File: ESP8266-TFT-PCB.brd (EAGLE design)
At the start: 38 x 50.8 mm, 5 parts

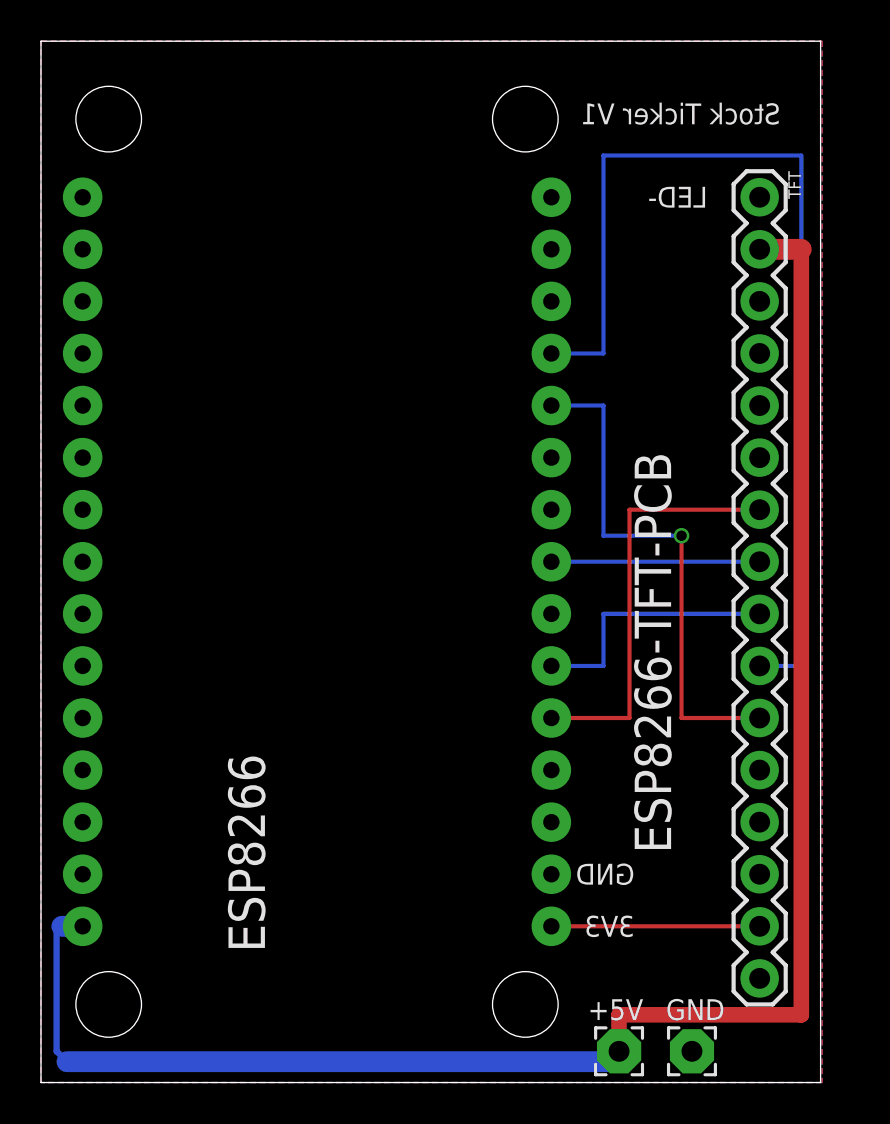
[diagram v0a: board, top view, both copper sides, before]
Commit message: Renamed and moved power connectors
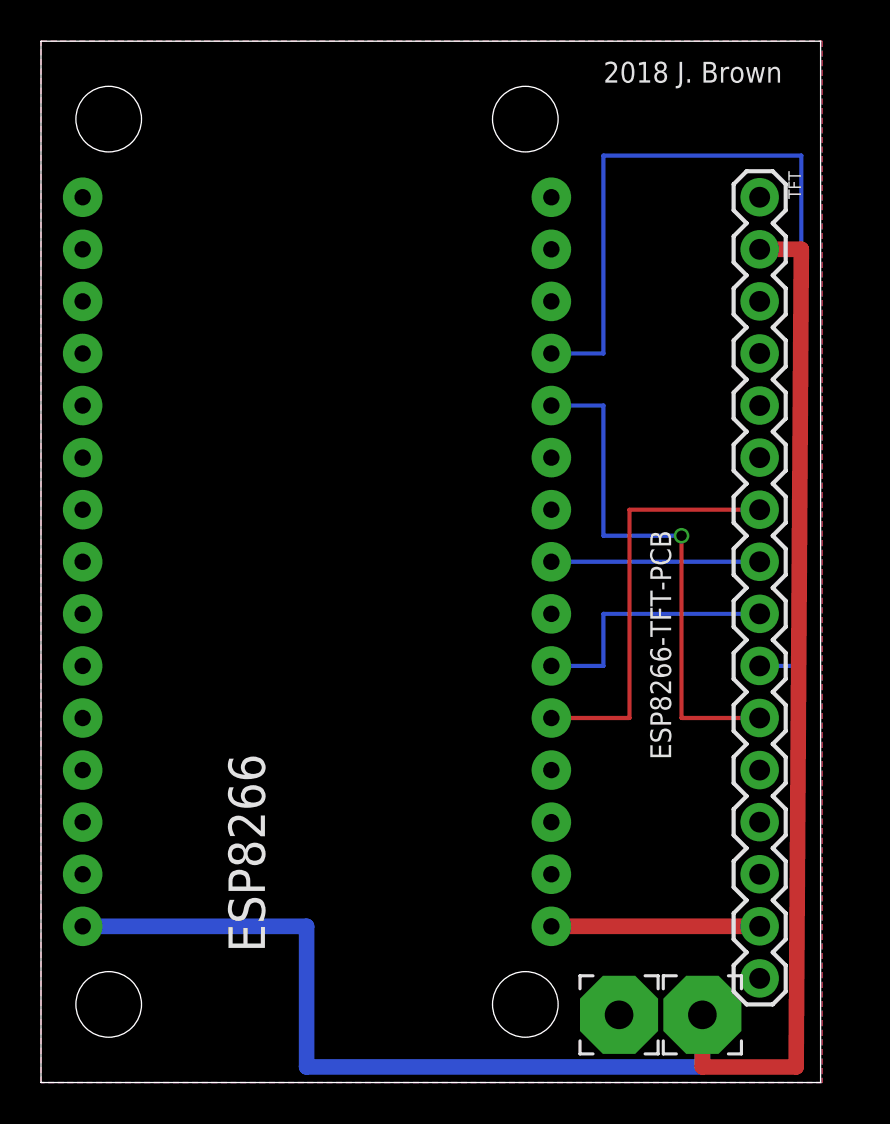
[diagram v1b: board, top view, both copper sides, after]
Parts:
- removed +5V: VCC, wirepad:2,15/1,0
- added VCC: +5V, wirepad:3,81/1,4
- GND: device wirepad:2,15/1,0 -> wirepad:3,81/1,4
- moved GND 3.98 mm to (36.3, 18.5)
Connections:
- net VCC: now also VCC.1; no longer +5V.1
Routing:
- net VCC: track 85.4 -> 88.6 mm
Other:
- board text removed: "Stock Ticker V1"
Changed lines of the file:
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@@
 <wire x1="46.152" y1="66.03" x2="8.128" y2="66.03" width="0" layer="20"/>
 <wire x1="8.128" y1="66.03" x2="8.128" y2="15.24" width="0" layer="20"/>
-<text x="44.196" y="63.754" size="1.016" layer="22" font="vector" rot="MR0">2018 J. Brown</text>
-<text x="44.196" y="61.976" size="1.016" layer="21" font="vector" rot="MR0">Stock Ticker V1</text>
-<text x="40.64" y="20.066" size="1.016" layer="22" font="vector" rot="MR0">GND</text>
-<text x="40.64" y="22.352" size="1.016" layer="22" font="vector" rot="MR0">VCC</text>
-<text x="40.64" y="32.512" size="1.016" layer="22" font="vector" rot="MR0">RST</text>
-<text x="40.64" y="35.052" size="1.016" layer="22" font="vector" rot="MR0">A0</text>
-<text x="40.64" y="42.672" size="1.016" layer="22" font="vector" rot="MR0">CS</text>
-<text x="40.64" y="40.132" size="1.016" layer="22" font="vector" rot="MR0">SCK</text>
-<text x="40.64" y="37.592" size="1.016" layer="22" font="vector" rot="MR0">SDA</text>
-<text x="40.64" y="55.372" size="1.016" layer="22" font="vector" rot="MR0">LED+</text>
-<text x="40.64" y="57.912" size="1.016" layer="21" font="vector" rot="MR0">LED-</text>
-<text x="34.798" y="18.288" size="1.016" layer="21" font="vector">+5V</text>
-<text x="38.608" y="18.288" size="1.016" layer="21" font="vector">GND</text>
+<text x="35.56" y="64.008" size="1.016" layer="21" font="vector">2018 J. Brown</text>
+<text x="38.862" y="30.988" size="1.016" layer="21" font="vector" rot="R90">ESP8266-TFT-PCB</text>
+<text x="41.148" y="19.812" size="1.016" layer="22" font="vector" rot="MR0">GND</text>
+<text x="41.148" y="22.352" size="1.016" layer="22" font="vector" rot="MR0">VCC</text>
+<text x="41.148" y="32.512" size="1.016" layer="22" font="vector" rot="MR0">RST</text>
+<text x="41.148" y="35.052" size="1.016" layer="22" font="vector" rot="MR0">A0</text>
+<text x="41.148" y="42.672" size="1.016" layer="22" font="vector" rot="MR0">CS</text>
+<text x="41.148" y="40.132" size="1.016" layer="22" font="vector" rot="MR0">SCK</text>
+<text x="41.148" y="37.592" size="1.016" layer="22" font="vector" rot="MR0">SDA</text>
+<text x="41.148" y="55.372" size="1.016" layer="22" font="vector" rot="MR0">LED+</text>
+<text x="41.148" y="57.912" size="1.016" layer="22" font="vector" rot="MR0">LED-</text>
+<text x="41.402" y="15.748" size="1.016" layer="22" font="vector" rot="MR0">+5V</text>
+<text x="37.338" y="15.748" size="1.016" layer="22" font="vector" rot="MR0">GND</text>
 <text x="14.986" y="24.892" size="1.016" layer="22" rot="MR0">GND</text>
 <text x="14.732" y="22.606" size="1.016" layer="22" font="vector" rot="MR0">VIN</text>
-<text x="37.084" y="22.352" size="1.016" layer="21" font="vector" rot="MR0">3V3</text>
-<text x="37.084" y="24.892" size="1.016" layer="21" font="vector" rot="MR0">GND</text>
-<text x="37.084" y="32.512" size="1.016" layer="22" font="vector" rot="MR0">D8</text>
-<text x="37.084" y="35.052" size="1.016" layer="22" rot="MR0">D7</text>
-<text x="37.084" y="37.592" size="1.016" layer="22" rot="MR0">D6</text>
-<text x="37.084" y="40.132" size="1.016" layer="22" rot="MR0">D5</text>
-<text x="37.084" y="48.006" size="1.016" layer="22" rot="MR0">D4</text>
-<text x="38.862" y="26.416" size="1.778" layer="21" rot="R90">ESP8266-TFT-PCB </text>
+<text x="37.338" y="22.352" size="1.016" layer="22" font="vector" rot="MR0">3V3</text>
+<text x="37.338" y="24.892" size="1.016" layer="22" font="vector" rot="MR0">GND</text>
+<text x="37.338" y="32.512" size="1.016" layer="22" font="vector" rot="MR0">D8</text>
+<text x="37.338" y="35.052" size="1.016" layer="22" rot="MR0">D7</text>
+<text x="37.338" y="37.592" size="1.016" layer="22" rot="MR0">D6</text>
+<text x="37.338" y="40.132" size="1.016" layer="22" rot="MR0">D5</text>
+<text x="37.338" y="47.752" size="1.016" layer="22" rot="MR0">D4</text>
 </plain>
 <attributes>
@@
 <elements>
 <element name="TFT" library="SparkFun-Connectors" package="1X16" value="0" x="43.18" y="58.42" rot="R270"/>
-<element name="ESP8266" library="ESP12E_DEVKIT" package="ESP12E_DEVKIT" value="ESP12E_DEVKIT" x="21.59" y="40.64"/>
+<element name="ESP8266" library="ESP12E_DEVKIT" package="ESP12E_DEVKIT" value="ESP12E_DEVKIT" x="21.59" y="40.64" smashed="yes">
+<attribute name="NAME" x="19.05" y="21.59" size="1.778" layer="25" rot="R90"/>
+<attribute name="VALUE" x="25.4" y="21.59" size="1.778" layer="27" rot="R90"/>
+</element>
 <element name="FRAME1" library="SparkFun-Aesthetics" package="CREATIVE_COMMONS" value="FRAME-LETTER" x="-21.59" y="-27.94"/>
-<element name="+5V" library="wirepad" library_urn="urn:adsk.eagle:library:412" package="2,15/1,0" package3d_urn="urn:adsk.eagle:package:30831/1" value="VCC" x="36.322" y="16.764" smashed="yes">
-<attribute name="VALUE" x="33.782" y="16.748" size="0.0254" layer="27"/>
+<element name="GND" library="wirepad" library_urn="urn:adsk.eagle:library:412" package="3,81/1,4" package3d_urn="urn:adsk.eagle:package:30835/1" value="GND" x="36.322" y="18.542" smashed="yes">
+<attribute name="VALUE" x="36.322" y="19.742" size="0.0254" layer="27"/>
 </element>
-<element name="GND" library="wirepad" library_urn="urn:adsk.eagle:library:412" package="2,15/1,0" package3d_urn="urn:adsk.eagle:package:30831/1" value="GND" x="39.878" y="16.764" smashed="yes">
-<attribute name="VALUE" x="39.878" y="17.764" size="0.0254" layer="27"/>
+<element name="VCC" library="wirepad" library_urn="urn:adsk.eagle:library:412" package="3,81/1,4" package3d_urn="urn:adsk.eagle:package:30835/1" value="+5V" x="40.386" y="18.542" smashed="yes">
+<attribute name="VALUE" x="40.386" y="19.742" size="0.0254" layer="27"/>
 </element>
 </elements>
@@
 <contactref element="TFT" pad="1"/>
 <contactref element="ESP8266" pad="GND@1"/>
-<contactref element="GND" pad="1"/>
 <contactref element="TFT" pad="16"/>
 <contactref element="ESP8266" pad="GND@3"/>
@@
 <vertex x="8.128" y="15.24"/>
 </polygon>
+<contactref element="GND" pad="1"/>
 </signal>
 <signal name="N$5">
@@
 <signal name="VCC">
 <contactref element="ESP8266" pad="VIN"/>
-<contactref element="+5V" pad="1"/>
 <contactref element="TFT" pad="2"/>
-<wire x1="43.18" y1="55.88" x2="45.212" y2="55.88" width="1.016" layer="1"/>
-<wire x1="45.212" y1="55.88" x2="45.212" y2="18.542" width="0.762" layer="1"/>
-<wire x1="36.322" y1="18.542" x2="36.322" y2="16.764" width="0.762" layer="1"/>
-<wire x1="45.212" y1="18.542" x2="36.322" y2="18.542" width="0.762" layer="1"/>
-<wire x1="10.16" y1="22.86" x2="9.144" y2="22.86" width="1.016" layer="16"/>
-<wire x1="9.144" y1="22.86" x2="8.89" y2="22.606" width="0.3048" layer="16"/>
-<wire x1="8.89" y1="22.606" x2="8.89" y2="16.764" width="0.3048" layer="16"/>
-<wire x1="8.89" y1="16.764" x2="9.398" y2="16.256" width="0.3048" layer="16"/>
-<wire x1="36.322" y1="16.256" x2="36.322" y2="16.764" width="0.3048" layer="16"/>
-<wire x1="9.398" y1="16.256" x2="36.322" y2="16.256" width="1.016" layer="16"/>
+<wire x1="43.18" y1="55.88" x2="45.212" y2="55.88" width="0.762" layer="1"/>
+<wire x1="44.958" y1="16.002" x2="45.212" y2="55.88" width="0.762" layer="1"/>
+<wire x1="10.16" y1="22.86" x2="21.082" y2="22.86" width="0.762" layer="16"/>
+<wire x1="21.082" y1="22.86" x2="21.082" y2="16.002" width="0.762" layer="16"/>
+<wire x1="21.082" y1="16.002" x2="40.386" y2="16.002" width="0.762" layer="16"/>
+<contactref element="VCC" pad="1"/>
+<wire x1="40.386" y1="18.542" x2="40.386" y2="16.002" width="0.762" layer="16"/>
+<wire x1="40.386" y1="18.542" x2="40.386" y2="16.002" width="0.762" layer="1"/>
+<wire x1="40.386" y1="16.002" x2="44.958" y2="16.002" width="0.762" layer="1"/>
 </signal>
 <signal name="N$1">
 <contactref element="ESP8266" pad="3V3@2"/>
 <contactref element="TFT" pad="15"/>
-<wire x1="43.18" y1="22.86" x2="33.02" y2="22.86" width="0.2032" layer="1"/>
+<wire x1="43.18" y1="22.86" x2="33.02" y2="22.86" width="0.762" layer="1"/>
 </signal>
 </signals>
